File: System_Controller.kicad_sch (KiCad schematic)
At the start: 49 parts, among them J10 CONSOLE, J11 USB_B_Micro, J12 Conn_ARM_JTAG_SWD_10, SW1 USB_PGM, SW2 USB_PGM, U16 RP2040, U17 IS25LP128F-JBLE, Y1 12MHz

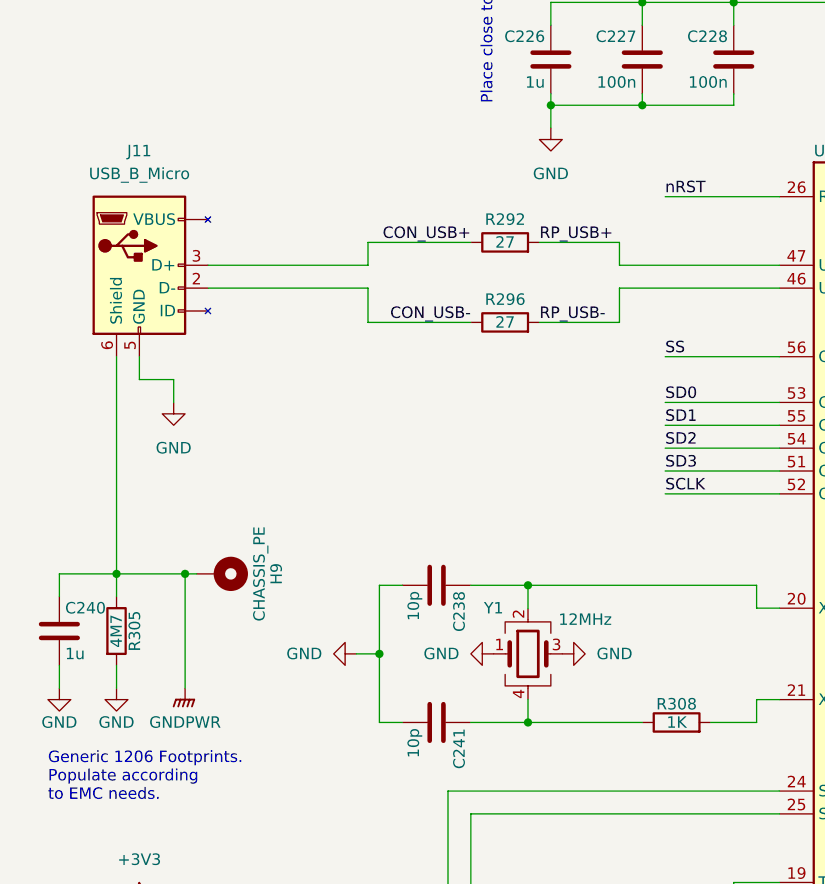
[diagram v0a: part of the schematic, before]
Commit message: Fixing termination for T1L PHYs
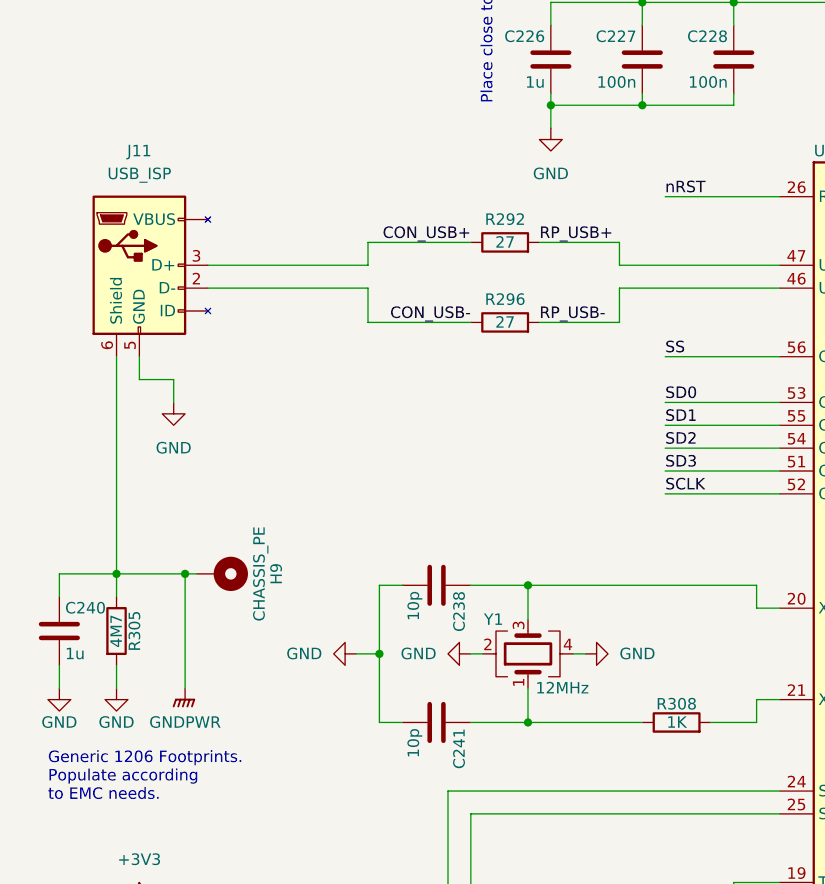
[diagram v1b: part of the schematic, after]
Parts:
- J11: value USB_B_Micro -> USB_ISP
- Y1: MPN (none) -> ABM8G-12.000MHZ-B4Y-T; ON_FARNELL (none) -> 2308707
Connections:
- net GND: now also Y1.2, Y1.4; no longer Y1.1, Y1.3
- net at C238.1, U16.20 (XIN): now also Y1.3; no longer Y1.2
- net at C241.1, R308.1: now also Y1.1; no longer Y1.4
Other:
- moved on the sheet: Y1
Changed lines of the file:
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@@
     (stroke (width 0) (type default) (color 0 0 0 0))
   )
-  (wire (pts (xy 71.12 118.11) (xy 71.12 115.57))
+  (wire (pts (xy 71.12 114.3) (xy 71.12 118.11))
     (stroke (width 0) (type default) (color 0 0 0 0))
   )
@@
     (stroke (width 0) (type default) (color 0 0 0 0))
   )
+  (wire (pts (xy 76.2 110.49) (xy 77.47 110.49))
+    (stroke (width 0) (type default) (color 0 0 0 0))
+  )
   (wire (pts (xy 149.86 62.23) (xy 194.31 62.23))
     (stroke (width 0) (type default) (color 0 0 0 0))
@@
     (stroke (width 0) (type default) (color 0 0 0 0))
   )
-  (wire (pts (xy 71.12 102.87) (xy 71.12 105.41))
+  (wire (pts (xy 71.12 102.87) (xy 71.12 106.68))
     (stroke (width 0) (type default) (color 0 0 0 0))
   )
@@
   )
   (wire (pts (xy 162.56 82.55) (xy 173.99 82.55))
+    (stroke (width 0) (type default) (color 0 0 0 0))
+  )
+  (wire (pts (xy 64.77 110.49) (xy 66.04 110.49))
     (stroke (width 0) (type default) (color 0 0 0 0))
   )
@@
     (in_bom yes) (on_board yes) (fields_autoplaced)
     (property "Reference" "J11" (id 0) (at 27.94 54.61 0))
-    (property "Value" "USB_B_Micro" (id 1) (at 27.94 57.15 0))
+    (property "Value" "USB_ISP" (id 1) (at 27.94 57.15 0))
     (property "Footprint" "Connector_USB:USB_Micro-B_Wuerth_614105150721_Vertical_CircularHoles" (id 2) (at 31.75 68.58 0)
       (effects (font (size 1.27 1.27)) hide)
@@
     (pin "2")
   )
-  (symbol (lib_id "Device:Crystal_GND24") (at 71.12 110.49 0) (unit 1)
-    (in_bom yes) (on_board yes)
-    (property "Reference" "Y1" (id 0) (at 67.31 105.41 0))
-    (property "Value" "12MHz" (id 1) (at 77.47 106.68 0))
+  (symbol (lib_id "Device:Crystal_GND24") (at 71.12 110.49 90) (unit 1)
+    (in_bom yes) (on_board yes)
+    (property "Reference" "Y1" (id 0) (at 67.31 106.68 90))
+    (property "Value" "12MHz" (id 1) (at 74.93 114.3 90))
     (property "Footprint" "Crystal:Crystal_SMD_Abracon_ABM8G-4Pin_3.2x2.5mm" (id 2) (at 71.12 110.49 0)
       (effects (font (size 1.27 1.27)) hide)
     )
-    (property "Datasheet" "~" (id 3) (at 71.12 110.49 0)
+    (property "Datasheet" "https://abracon.com/Resonators/ABM8G.pdf" (id 3) (at 71.12 110.49 0)
+      (effects (font (size 1.27 1.27)) hide)
+    )
+    (property "MPN" "ABM8G-12.000MHZ-B4Y-T" (id 4) (at 71.12 110.49 0)
+      (effects (font (size 1.27 1.27)) hide)
+    )
+    (property "ON_FARNELL" "2308707" (id 5) (at 71.12 110.49 0)
       (effects (font (size 1.27 1.27)) hide)
     )
@@
       (effects (font (size 1.27 1.27)) hide)
     )
-    (property "Datasheet" "" (id 3) (at 252.73 128.27 0)
+    (property "Datasheet" "https://www.issi.com/WW/pdf/25LP-WP128F.pdf" (id 3) (at 252.73 128.27 0)
       (effects (font (size 1.27 1.27)) hide)
     )
@@
     (pin "2")
   )
-  (symbol (lib_id "power:GND") (at 67.31 110.49 270) (unit 1)
+  (symbol (lib_id "power:GND") (at 64.77 110.49 270) (unit 1)
     (in_bom yes) (on_board yes) (fields_autoplaced)
-    (property "Reference" "#PWR0231" (id 0) (at 60.96 110.49 0)
-      (effects (font (size 1.27 1.27)) hide)
-    )
-    (property "Value" "GND" (id 1) (at 63.5 110.4899 90)
+    (property "Reference" "#PWR0231" (id 0) (at 58.42 110.49 0)
+      (effects (font (size 1.27 1.27)) hide)
+    )
+    (property "Value" "GND" (id 1) (at 60.96 110.4899 90)
       (effects (font (size 1.27 1.27)) (justify right))
     )
-    (property "Footprint" "" (id 2) (at 67.31 110.49 0)
-      (effects (font (size 1.27 1.27)) hide)
-    )
-    (property "Datasheet" "" (id 3) (at 67.31 110.49 0)
+    (property "Footprint" "" (id 2) (at 64.77 110.49 0)
+      (effects (font (size 1.27 1.27)) hide)
+    )
+    (property "Datasheet" "" (id 3) (at 64.77 110.49 0)
       (effects (font (size 1.27 1.27)) hide)
     )
@@
     (pin "2")
   )
-  (symbol (lib_id "power:GND") (at 74.93 110.49 90) (unit 1)
+  (symbol (lib_id "power:GND") (at 77.47 110.49 90) (unit 1)
     (in_bom yes) (on_board yes) (fields_autoplaced)
-    (property "Reference" "#PWR0232" (id 0) (at 81.28 110.49 0)
-      (effects (font (size 1.27 1.27)) hide)
-    )
-    (property "Value" "GND" (id 1) (at 78.74 110.4899 90)
+    (property "Reference" "#PWR0232" (id 0) (at 83.82 110.49 0)
+      (effects (font (size 1.27 1.27)) hide)
+    )
+    (property "Value" "GND" (id 1) (at 81.28 110.4899 90)
       (effects (font (size 1.27 1.27)) (justify right))
     )
-    (property "Footprint" "" (id 2) (at 74.93 110.49 0)
-      (effects (font (size 1.27 1.27)) hide)
-    )
-    (property "Datasheet" "" (id 3) (at 74.93 110.49 0)
-      (effects (font (size 1.27 1.27)) hide)
-    )
+    (property "Footprint" "" (id 2) (at 77.47 110.49 0)
+      (effects (font (size 1.27 1.27)) hide)
+    )
+    (property "Datasheet" "" (id 3) (at 77.47 110.49 0)
+      (effects (font (size 1.27 1.27)) hide)
+    )

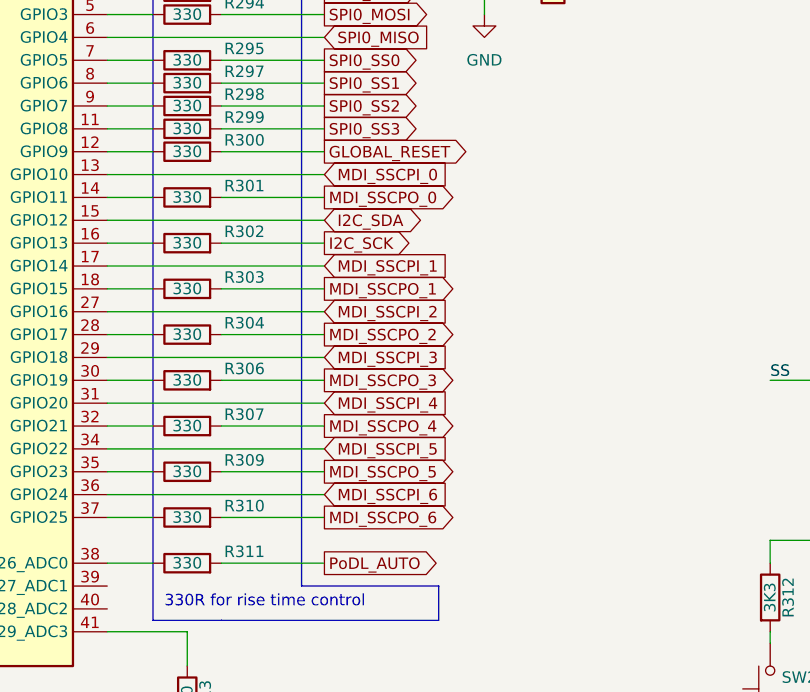
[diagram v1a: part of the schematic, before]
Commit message: Correcting SCCP spelling
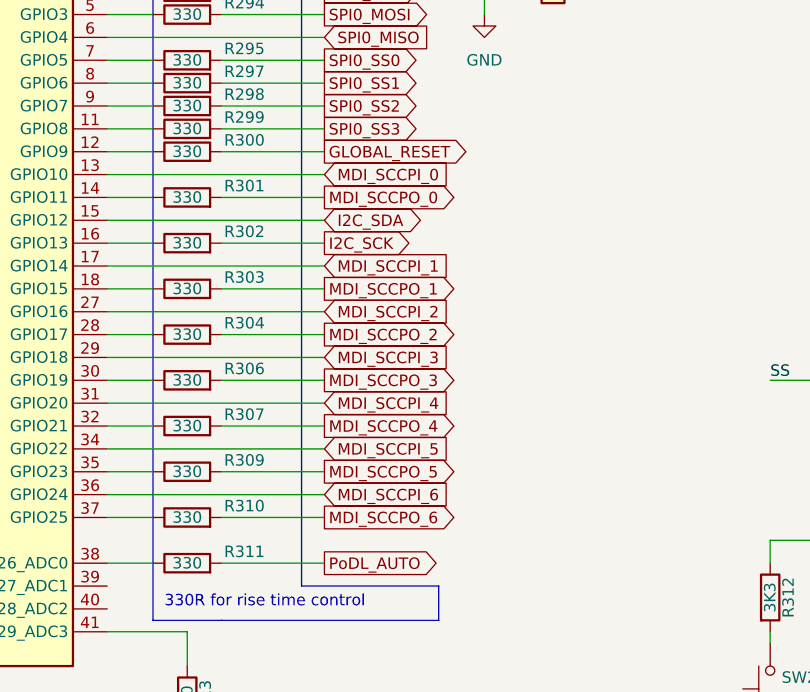
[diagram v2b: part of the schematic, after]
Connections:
- net MDI_SSCPI_0 renamed MDI_SCCPI_0
- net MDI_SSCPI_1 renamed MDI_SCCPI_1
- net MDI_SSCPI_2 renamed MDI_SCCPI_2
- net MDI_SSCPI_3 renamed MDI_SCCPI_3
- net MDI_SSCPI_4 renamed MDI_SCCPI_4
- net MDI_SSCPI_5 renamed MDI_SCCPI_5
- net MDI_SSCPI_6 renamed MDI_SCCPI_6
- net MDI_SSCPO_0 renamed MDI_SCCPO_0
- net MDI_SSCPO_1 renamed MDI_SCCPO_1
- net MDI_SSCPO_2 renamed MDI_SCCPO_2
- net MDI_SSCPO_3 renamed MDI_SCCPO_3
- net MDI_SSCPO_4 renamed MDI_SCCPO_4
- net MDI_SSCPO_5 renamed MDI_SCCPO_5
- net MDI_SSCPO_6 renamed MDI_SCCPO_6
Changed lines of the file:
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@@
     (effects (font (size 1.27 1.27)) (justify left bottom))
   )
-  (global_label "MDI_SSCPI_2" (shape input) (at 173.99 100.33 0) (fields_autoplaced)
+  (global_label "MDI_SCCPI_2" (shape input) (at 173.99 100.33 0) (fields_autoplaced)
     (effects (font (size 1.27 1.27)) (justify left))
     (property "Intersheet References" "${INTERSHEET_REFS}" (id 0) (at 188.4379 100.2506 0)
@@
     )
   )
-  (global_label "MDI_SSCPO_4" (shape output) (at 173.99 113.03 0) (fields_autoplaced)
+  (global_label "MDI_SCCPO_4" (shape output) (at 173.99 113.03 0) (fields_autoplaced)
     (effects (font (size 1.27 1.27)) (justify left))
     (property "Intersheet References" "${INTERSHEET_REFS}" (id 0) (at 189.1636 112.9506 0)
@@
     )
   )
-  (global_label "MDI_SSCPO_2" (shape output) (at 173.99 102.87 0) (fields_autoplaced)
+  (global_label "MDI_SCCPO_2" (shape output) (at 173.99 102.87 0) (fields_autoplaced)
     (effects (font (size 1.27 1.27)) (justify left))
     (property "Intersheet References" "${INTERSHEET_REFS}" (id 0) (at 189.1636 102.7906 0)
@@
     )
   )
-  (global_label "MDI_SSCPI_1" (shape input) (at 173.99 95.25 0) (fields_autoplaced)
+  (global_label "MDI_SCCPI_1" (shape input) (at 173.99 95.25 0) (fields_autoplaced)
     (effects (font (size 1.27 1.27)) (justify left))
     (property "Intersheet References" "${INTERSHEET_REFS}" (id 0) (at 188.4379 95.1706 0)
@@
     )
   )
-  (global_label "MDI_SSCPI_4" (shape input) (at 173.99 110.49 0) (fields_autoplaced)
+  (global_label "MDI_SCCPI_4" (shape input) (at 173.99 110.49 0) (fields_autoplaced)
     (effects (font (size 1.27 1.27)) (justify left))
     (property "Intersheet References" "${INTERSHEET_REFS}" (id 0) (at 188.4379 110.4106 0)
@@
     )
   )
-  (global_label "MDI_SSCPO_1" (shape output) (at 173.99 97.79 0) (fields_autoplaced)
+  (global_label "MDI_SCCPO_1" (shape output) (at 173.99 97.79 0) (fields_autoplaced)
     (effects (font (size 1.27 1.27)) (justify left))
     (property "Intersheet References" "${INTERSHEET_REFS}" (id 0) (at 189.1636 97.7106 0)
@@
     )
   )
-  (global_label "MDI_SSCPI_6" (shape input) (at 173.99 120.65 0) (fields_autoplaced)
+  (global_label "MDI_SCCPI_6" (shape input) (at 173.99 120.65 0) (fields_autoplaced)
     (effects (font (size 1.27 1.27)) (justify left))
     (property "Intersheet References" "${INTERSHEET_REFS}" (id 0) (at 188.4379 120.5706 0)
@@
     )
   )
-  (global_label "MDI_SSCPO_0" (shape output) (at 173.99 87.63 0) (fields_autoplaced)
+  (global_label "MDI_SCCPO_0" (shape output) (at 173.99 87.63 0) (fields_autoplaced)
     (effects (font (size 1.27 1.27)) (justify left))
     (property "Intersheet References" "${INTERSHEET_REFS}" (id 0) (at 189.1636 87.5506 0)
@@
     )
   )
-  (global_label "MDI_SSCPO_3" (shape output) (at 173.99 107.95 0) (fields_autoplaced)
+  (global_label "MDI_SCCPO_3" (shape output) (at 173.99 107.95 0) (fields_autoplaced)
     (effects (font (size 1.27 1.27)) (justify left))
     (property "Intersheet References" "${INTERSHEET_REFS}" (id 0) (at 189.1636 107.8706 0)
@@
     )
   )
-  (global_label "MDI_SSCPO_5" (shape output) (at 173.99 118.11 0) (fields_autoplaced)
+  (global_label "MDI_SCCPO_5" (shape output) (at 173.99 118.11 0) (fields_autoplaced)
     (effects (font (size 1.27 1.27)) (justify left))
     (property "Intersheet References" "${INTERSHEET_REFS}" (id 0) (at 189.1636 118.0306 0)
@@
     )
   )
-  (global_label "MDI_SSCPO_6" (shape output) (at 173.99 123.19 0) (fields_autoplaced)
+  (global_label "MDI_SCCPO_6" (shape output) (at 173.99 123.19 0) (fields_autoplaced)
     (effects (font (size 1.27 1.27)) (justify left))
     (property "Intersheet References" "${INTERSHEET_REFS}" (id 0) (at 189.1636 123.1106 0)
@@
     )
   )
-  (global_label "MDI_SSCPI_0" (shape input) (at 173.99 85.09 0) (fields_autoplaced)
+  (global_label "MDI_SCCPI_0" (shape input) (at 173.99 85.09 0) (fields_autoplaced)
     (effects (font (size 1.27 1.27)) (justify left))
     (property "Intersheet References" "${INTERSHEET_REFS}" (id 0) (at 188.4379 85.0106 0)
@@
     )
   )
-  (global_label "MDI_SSCPI_5" (shape input) (at 173.99 115.57 0) (fields_autoplaced)
+  (global_label "MDI_SCCPI_5" (shape input) (at 173.99 115.57 0) (fields_autoplaced)
     (effects (font (size 1.27 1.27)) (justify left))
     (property "Intersheet References" "${INTERSHEET_REFS}" (id 0) (at 188.4379 115.4906 0)
@@
     )
   )
-  (global_label "MDI_SSCPI_3" (shape input) (at 173.99 105.41 0) (fields_autoplaced)
+  (global_label "MDI_SCCPI_3" (shape input) (at 173.99 105.41 0) (fields_autoplaced)
     (effects (font (size 1.27 1.27)) (justify left))
     (property "Intersheet References" "${INTERSHEET_REFS}" (id 0) (at 188.4379 105.3306 0)
